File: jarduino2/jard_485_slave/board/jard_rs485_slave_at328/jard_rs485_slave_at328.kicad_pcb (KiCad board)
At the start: 2 copper layers, 80 x 30 mm, 66 parts, among them J1 BUS_IN, J2 BUS_OUT, J3 Débit, J4 Niveaux, J6 EV1, J7 ISCP, Q4 BPC_FMMT38C, Q6 BPC_IPP034N03L, U1 BPC_Alim5V, U2 MAX485E, U5 ATmega328P-A, U6 BPC_DHT22, Y1 Resonator

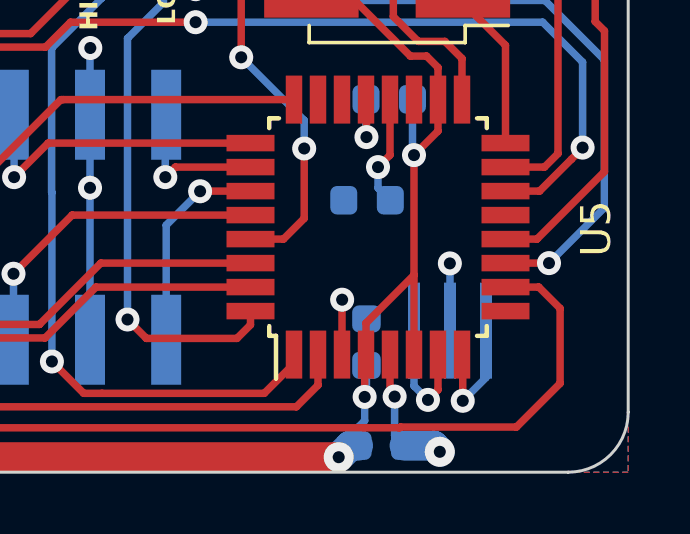
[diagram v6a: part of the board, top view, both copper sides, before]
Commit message: Correction empreinte résonateur
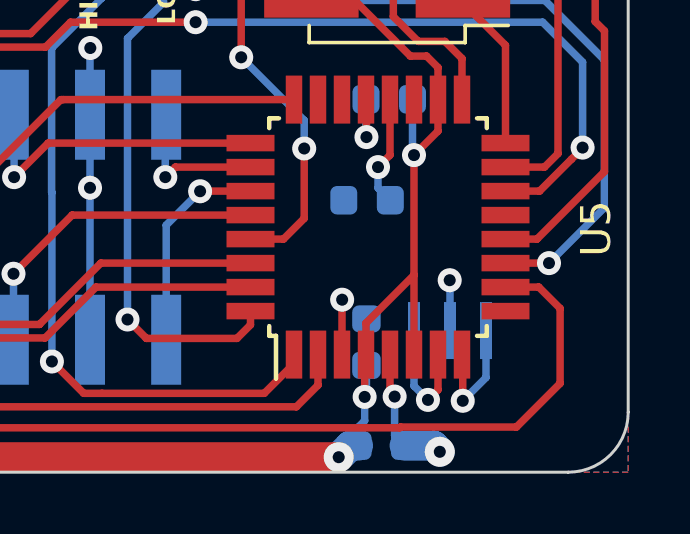
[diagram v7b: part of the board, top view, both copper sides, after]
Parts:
- Y1: footprint Crystal:Resonator_SMD_Murata_CSTxExxV-3Pin_3.0x1.1mm_HandSoldering -> bpc:BPC_16MHz_CSTNE16M0V530000R0
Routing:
- net GND: track 55.7 -> 55.2 mm
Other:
- board text added: "01/04/2024"
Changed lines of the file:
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@@
   (title_block
     (title "Carte de commande d'un OYA - Esclave RS485")
-    (date "2024-03-31")
+    (date "2024-04-01")
     (rev "D0")
     (company "BPC")
@@
     (descr "32-Lead Plastic Thin Quad Flatpack (PT) - 7x7x1.0 mm Body, 2.00 mm [TQFP] (see Microchip Packaging Specification 00000049BS.pdf)")
     (tags "QFP 0.8")
+    (property "Fabricant" "Microchip: ATMEGA328P-AN")
+    (property "Fournisseur" "Farnell: 2443178")
     (property "Sheetfile" "uc.kicad_sch")
     (property "Sheetname" "UC")
@@
     )
   )
-  (footprint "Crystal:Resonator_SMD_Murata_CSTxExxV-3Pin_3.0x1.1mm_HandSoldering" (layer "B.Cu")
+  (footprint "bpc:BPC_16MHz_CSTNE16M0V530000R0" (layer "B.Cu")
     (at 124.06 65.28 180)
-    (descr "SMD Resomator/Filter Murata CSTCE, https://www.murata.com/en-eu/products/productdata/8801162264606/SPEC-CSTNE16M0VH3C000R0.pdf")
-    (tags "SMD SMT ceramic resonator filter")
+    (property "Availability" "In Stock")
+    (property "Check_prices" "https://www.snapeda.com/parts/CSTNE16M0V530000R0/Murata+Electronics+North+America/view-part/?ref=eda")
+    (property "Description" "\n16 MHz Ceramic Resonator Built in Capacitor 15 pF ±0.3% 40 Ohms -40°C ~ 85°C Surface Mount\n")
+    (property "Fabricant" "Murata: CSTNE16M0V530000R0")
+    (property "Fournisseur" "Farnell: 4127618")
+    (property "MANUFACTURER" "Murata")
+    (property "MAXIMUM_PACKAGE_HEIGHT" "1mm")
+    (property "MF" "Murata Electronics")
+    (property "MP" "CSTNE16M0V530000R0")
+    (property "PARTREV" "JGC42-8853B")
+    (property "Package" "SMD-3 Murata")
+    (property "Price" "None")
+    (property "Purchase-URL" "https://www.snapeda.com/api/url_track_click_mouser/?unipart_id=2773601&manufacturer=Murata Electronics&part_name=CSTNE16M0V530000R0&search_term=None")
+    (property "STANDARD" "Manufacturer Recomendations")
     (property "Sheetfile" "uc.kicad_sch")
     (property "Sheetname" "UC")
-    (property "ki_description" "Three pin ceramic resonator")
-    (property "ki_keywords" "ceramic resonator")
+    (property "SnapEDA_Link" "https://www.snapeda.com/parts/CSTNE16M0V530000R0/Murata+Electronics+North+America/view-part/?ref=snap")
+    (property "ki_description" "Resonateur 16MHz (pour Arduino)")
     (attr smd)
-    (fp_text reference "Y1" (at 0 2.45) (layer "B.SilkS")
-        (effects (font (size 1 1) (thickness 0.15)) (justify mirror))
-    )
-    (fp_text value "Resonator" (at 0 -1.8) (layer "B.Fab")
-        (effects (font (size 0.2 0.2) (thickness 0.03)) (justify mirror))
+    (fp_text reference "Y1" (at 0.032 1.7064) (layer "B.SilkS")
+        (effects (font (size 0.64 0.64) (thickness 0.15)) (justify mirror))
     )
-    (fp_text user "${REFERENCE}" (at 0.1 0.05) (layer "B.Fab")
-        (effects (font (size 0.6 0.6) (thickness 0.08)) (justify mirror))
+    (fp_text value "Resonator" (at 6.9408 -1.7064) (layer "B.Fab")
+        (effects (font (size 0.64 0.64) (thickness 0.15)) (justify mirror))
     )
-    (fp_line (start -2 -0.8) (end -2 -1.2)
-      (stroke (width 0.12) (type solid)) (layer "B.SilkS"))
-    (fp_line (start -2 1.2) (end -2 -0.8)
-      (stroke (width 0.12) (type solid)) (layer "B.SilkS"))
-    (fp_line (start -1.8 -1.2) (end -1.65 -1.2)
-      (stroke (width 0.12) (type solid)) (layer "B.SilkS"))
-    (fp_line (start -1.8 -0.8) (end -1.8 -1.2)
-      (stroke (width 0.12) (type solid)) (layer "B.SilkS"))
-    (fp_line (start -1.8 -0.8) (end -1.8 1.2)
-      (stroke (width 0.12) (type solid)) (layer "B.SilkS"))
-    (fp_line (start -1.8 1.2) (end -1.65 1.2)
-      (stroke (width 0.12) (type solid)) (layer "B.SilkS"))
-    (fp_line (start -0.75 -1.2) (end -0.8 -1.2)
-      (stroke (width 0.12) (type solid)) (layer "B.SilkS"))
-    (fp_line (start -0.75 -1.2) (end -0.75 -1.6)
-      (stroke (width 0.12) (type solid)) (layer "B.SilkS"))
-    (fp_line (start 1.8 -1.2) (end 1.65 -1.2)
-      (stroke (width 0.12) (type solid)) (layer "B.SilkS"))
-    (fp_line (start 1.8 -0.8) (end 1.8 -1.2)
-      (stroke (width 0.12) (type solid)) (layer "B.SilkS"))
-    (fp_line (start 1.8 1.2) (end 1.65 1.2)
-      (stroke (width 0.12) (type solid)) (layer "B.SilkS"))
-    (fp_line (start 1.8 1.2) (end 1.8 -0.8)
-      (stroke (width 0.12) (type solid)) (layer "B.SilkS"))
-    (fp_line (start -1.75 -1.85) (end -1.75 1.85)
+    (fp_line (start -1.72 0.65) (end -1.72 -0.65)
+      (stroke (width 0.127) (type solid)) (layer "B.SilkS"))
+    (fp_line (start 1.72 0.65) (end 1.72 -0.65)
+      (stroke (width 0.127) (type solid)) (layer "B.SilkS"))
+    (fp_circle (center -2.22 0) (end -2.12 0)
+      (stroke (width 0.2) (type solid)) (fill none) (layer "B.SilkS"))
+    (fp_line (start -1.85 -1.2) (end -1.85 1.2)
       (stroke (width 0.05) (type solid)) (layer "B.CrtYd"))
-    (fp_line (start -1.75 1.85) (end 1.75 1.85)
+    (fp_line (start -1.85 1.2) (end 1.85 1.2)
       (stroke (width 0.05) (type solid)) (layer "B.CrtYd"))
-    (fp_line (start 1.75 -1.85) (end -1.75 -1.85)
+    (fp_line (start 1.85 -1.2) (end -1.85 -1.2)
       (stroke (width 0.05) (type solid)) (layer "B.CrtYd"))
-    (fp_line (start 1.75 1.85) (end 1.75 -1.85)
+    (fp_line (start 1.85 1.2) (end 1.85 -1.2)
       (stroke (width 0.05) (type solid)) (layer "B.CrtYd"))
-    (fp_line (start -1.5 -0.3) (end -1.5 0.8)
-      (stroke (width 0.1) (type solid)) (layer "B.Fab"))
-    (fp_line (start -1 -0.8) (end -1.5 -0.3)
-      (stroke (width 0.1) (type solid)) (layer "B.Fab"))
-    (fp_line (start -1 -0.8) (end 1.5 -0.8)
-      (stroke (width 0.1) (type solid)) (layer "B.Fab"))
-    (fp_line (start 1.5 -0.8) (end 1.5 0.8)
-      (stroke (width 0.1) (type solid)) (layer "B.Fab"))
-    (fp_line (start 1.5 0.8) (end -1.5 0.8)
-      (stroke (width 0.1) (type solid)) (layer "B.Fab"))
-    (pad "1" smd rect (at -1.2 0 180) (size 0.4 3.2) (layers "B.Cu" "B.Paste" "B.Mask")
-      (net 40 "Net-(U5-XTAL2{slash}PB7)") (pinfunction "1") (pintype "passive"))
-    (pad "2" smd rect (at 0 0 180) (size 0.4 3.2) (layers "B.Cu" "B.Paste" "B.Mask")
-      (net 2 "GND") (pinfunction "2") (pintype "passive"))
-    (pad "3" smd rect (at 1.2 0 180) (size 0.4 3.2) (layers "B.Cu" "B.Paste" "B.Mask")
-      (net 41 "Net-(U5-XTAL1{slash}PB6)") (pinfunction "3") (pintype "passive"))
-    (model "${KICAD6_3DMODEL_DIR}/Crystal.3dshapes/Resonator_SMD_Murata_CSTxExxV-3Pin_3.0x1.1mm.wrl"
+    (fp_line (start -1.6 0.65) (end -1.6 -0.65)
+      (stroke (width 0.127) (type solid)) (layer "B.Fab"))
+    (fp_line (start -1.6 0.65) (end 1.6 0.65)
+      (stroke (width 0.127) (type solid)) (layer "B.Fab"))
+    (fp_line (start 1.6 -0.65) (end -1.6 -0.65)
+      (stroke (width 0.127) (type solid)) (layer "B.Fab"))
+    (fp_line (start 1.6 0.65) (end 1.6 -0.65)
+      (stroke (width 0.127) (type solid)) (layer "B.Fab"))
+    (fp_circle (center -2.22 0) (end -2.12 0)
+      (stroke (width 0.2) (type solid)) (fill none) (layer "B.Fab"))
+    (pad "1" smd rect (at -1.2 0 180) (size 0.4 1.9) (layers "B.Cu" "B.Paste" "B.Mask")
+      (net 40 "Net-(U5-XTAL2{slash}PB7)") (pintype "input") (solder_mask_margin 0.102))
+    (pad "2" smd rect (at 0 0 180) (size 0.4 1.9) (layers "B.Cu" "B.Paste" "B.Mask")
+      (net 2 "GND") (pintype "power_in") (solder_mask_margin 0.102))
+    (pad "3" smd rect (at 1.2 0 180) (size 0.4 1.9) (layers "B.Cu" "B.Paste" "B.Mask")
+      (net 41 "Net-(U5-XTAL1{slash}PB6)") (pintype "output") (solder_mask_margin 0.102))
+    (model "${BPCLIBS}/bpc/3d/CSTNE16M0V530000R0.step"
       (offset (xyz 0 0 0))
       (scale (xyz 1 1 1))
-      (rotate (xyz 0 0 0))
+      (rotate (xyz -90 0 0))
     )
   )
@@
   (gr_rect (start 50 40) (end 130 70)
     (stroke (width 0.1) (type solid)) (fill none) (layer "User.1"))
+  (gr_text "01/04/2024" (at 105.59 69.41) (layer "B.SilkS")
+    (effects (font (size 0.8 0.8) (thickness 0.1)) (justify left bottom mirror))
+  )
   (gr_text "Esclave OYA\nRev D0\nBPC 2024" (at 105.77 65.75) (layer "B.SilkS")
     (effects (font (size 1 1) (thickness 0.15)) (justify left bottom mirror))
@@
   (via (at 94.03 60.16) (size 0.8) (drill 0.4) (layers "F.Cu" "B.Cu") (net 2))
   (via (at 112.07 55.86) (size 0.8) (drill 0.4) (layers "F.Cu" "B.Cu") (net 2))
-  (via (at 124.055 63.04) (size 0.8) (drill 0.4) (layers "F.Cu" "B.Cu") (net 2))
+  (via (at 124.05 63.6) (size 0.8) (drill 0.4) (layers "F.Cu" "B.Cu") (net 2))
   (via (at 93.18 42.2) (size 0.8) (drill 0.4) (layers "F.Cu" "B.Cu") (net 2))
   (via (at 120.465 64.25) (size 0.8) (drill 0.4) (layers "F.Cu" "B.Cu") (net 2))
@@
   (segment (start 80.96 52.81) (end 80.12 52.81) (width 0.25) (layer "B.Cu") (net 2))
   (segment (start 112.06 58.085) (end 112.06 55.87) (width 0.25) (layer "B.Cu") (net 2))
-  (segment (start 124.06 63.045) (end 124.055 63.04) (width 0.25) (layer "B.Cu") (net 2))
   (segment (start 67.43 49.61) (end 67.43 48.57) (width 0.25) (layer "B.Cu") (net 2))
-  (segment (start 124.06 65.28) (end 124.06 63.045) (width 0.25) (layer "B.Cu") (net 2))
   (segment (start 70.01 64.49) (end 69.99 64.51) (width 0.25) (layer "B.Cu") (net 2))
   (segment (start 112.06 60.52) (end 112.06 58.085) (width 0.25) (layer "B.Cu") (net 2))
@@
   (segment (start 70.845 49.76) (end 71.42 49.76) (width 0.25) (layer "B.Cu") (net 2))
   (segment (start 109.47 53.36) (end 110.52 53.36) (width 0.25) (layer "B.Cu") (net 2))
+  (segment (start 124.06 63.61) (end 124.05 63.6) (width 0.25) (layer "B.Cu") (net 2))
   (segment (start 123.515 69.115) (end 123.72 69.32) (width 1) (layer "B.Cu") (net 2))
   (segment (start 122.214015 68.784015) (end 122.545 69.115) (width 0.25) (layer "B.Cu") (net 2))
+  (segment (start 124.06 65.28) (end 124.06 63.61) (width 0.25) (layer "B.Cu") (net 2))
   (segment (start 80.12 52.81) (end 79.4 52.09) (width 0.25) (layer "B.Cu") (net 2))
   (segment (start 84.14 54.81) (end 84.43 55.1) (width 0.25) (layer "B.Cu") (net 2))

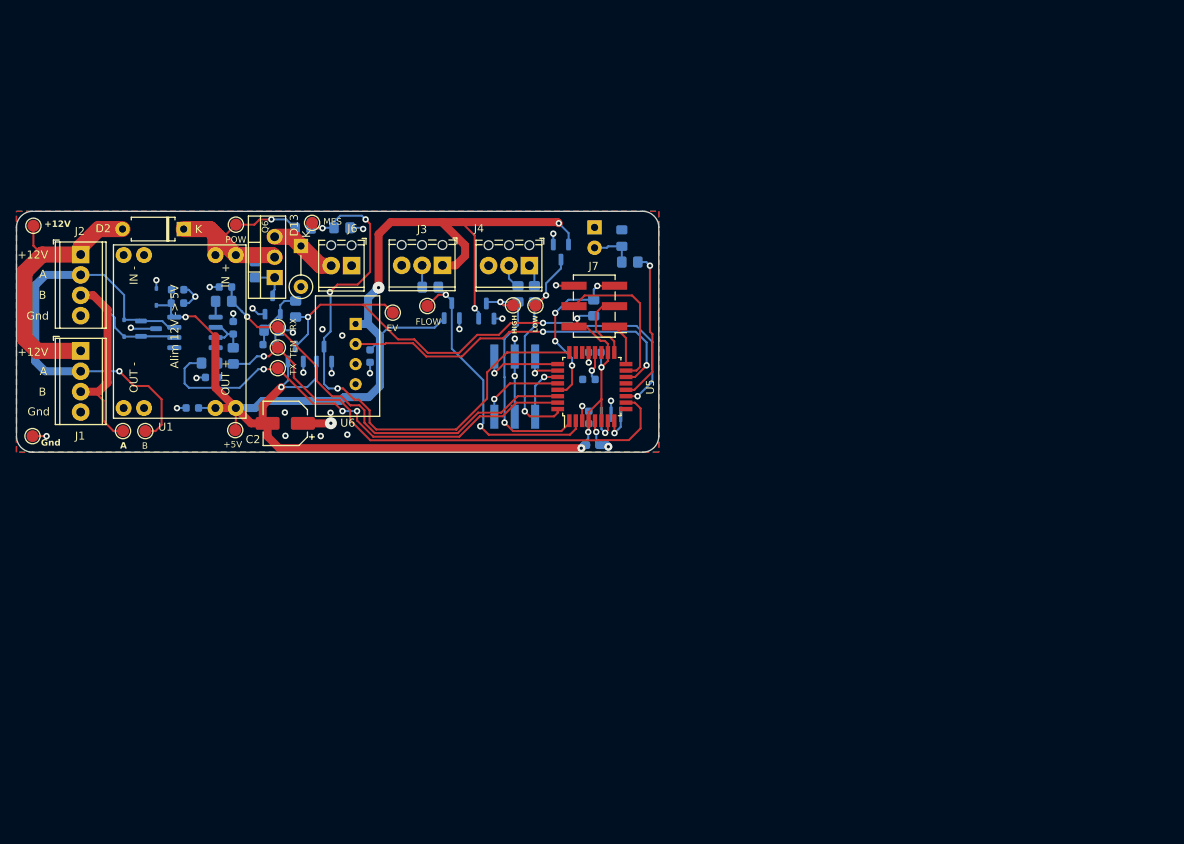
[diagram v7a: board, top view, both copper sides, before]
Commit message: Correction erreur de MOS (N au lieu de P) + Saisie complete de la BOM
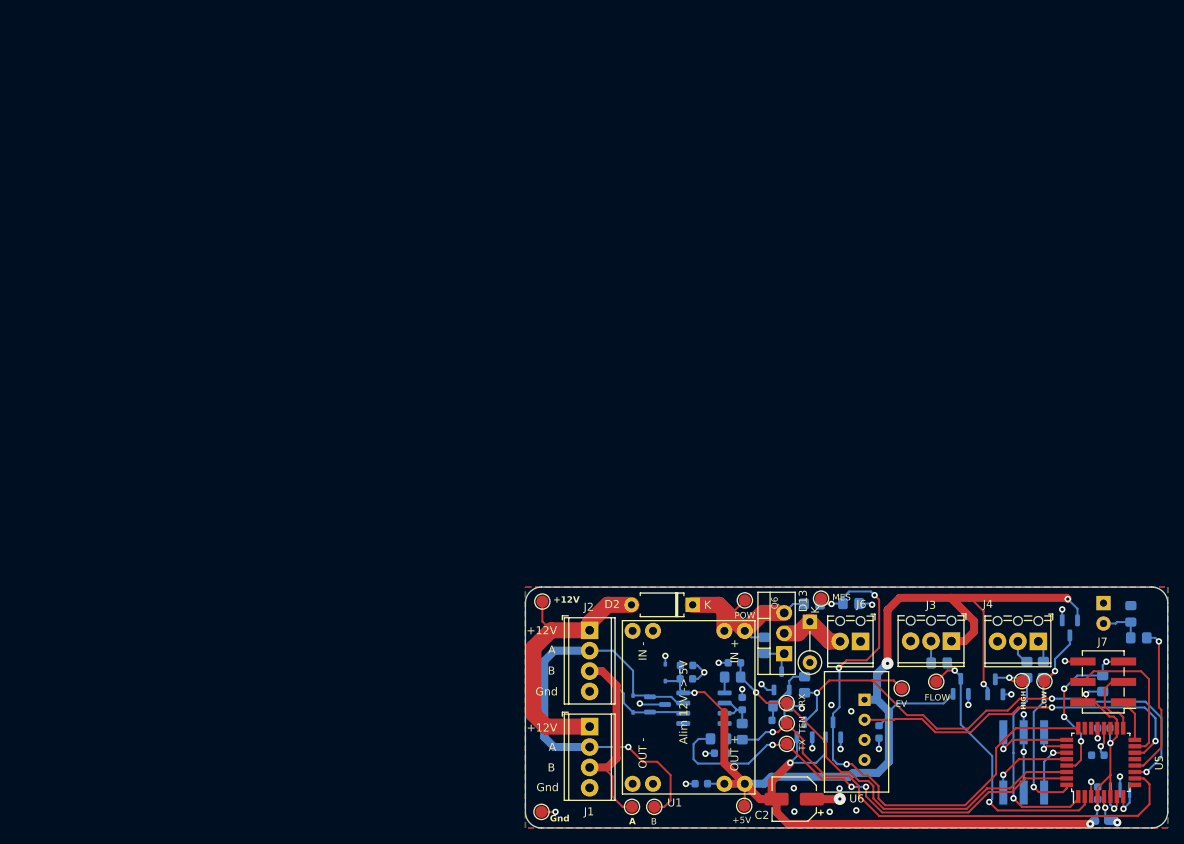
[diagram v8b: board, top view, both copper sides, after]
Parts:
- Q6: value BPC_IPP034N03L -> P03P4L-04
- moved Q6 78.9 mm to (145.6, 95.1)
- moved C3 78.8 mm to (133.5, 96.6)
- moved C4 78.8 mm to (133.4, 98.2)
- moved C5 78.8 mm to (185.2, 115.9)
- moved C6 78.8 mm to (144.9, 103.4)
- moved C8 78.8 mm to (185.4, 104.4)
- moved D11 78.8 mm to (126.8, 101.4)
- moved D15 78.8 mm to (129.8, 101.4)
- moved D2 78.8 mm to (134.2, 89.0)
- moved D8 78.8 mm to (167.6, 99.2)
- moved J1 78.8 mm to (121.4, 104.2)
- moved J2 78.8 mm to (121.4, 92.2)
- moved J4 78.8 mm to (177.3, 93.6)
- moved R12 78.8 mm to (189.8, 93.1)
- moved R17 78.8 mm to (143.1, 94.1)
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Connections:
- Q6 pad 2: POWER_12V -> Net-(D13-K)
- Q6 pad 3: Net-(D13-K) -> POWER_12V
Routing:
- net POWER_12V: track 30.6 -> 26.4 mm, vias 1 -> 0
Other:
- board text added: "02/04/2024"
- board text added: "Esclave OYA Rev E0 BPC 2024"
- board text removed: "01/04/2024"
- board text removed: "Esclave OYA Rev D0 BPC 2024"
